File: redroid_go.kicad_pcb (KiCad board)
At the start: 2 copper layers, 70 x 95 mm, 100 parts, among them J1 USB4105-GF-A, J2 5051101892, J3 Conn_01x02_Pin, J4 Conn_01x10_Pin, Q1 UMH3N, Q2 PMOS, Q3 UMH3N, SW1 UP, SW10 A, SW11 SW_SPDT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

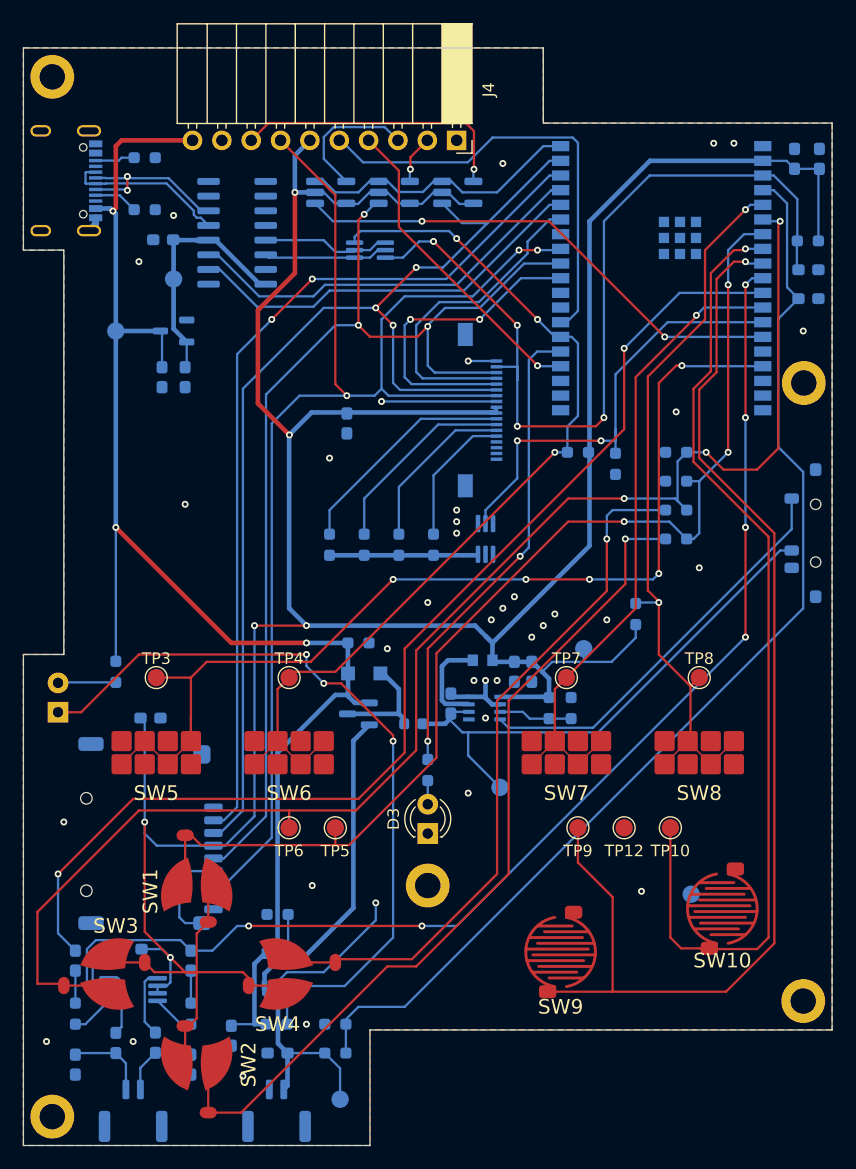
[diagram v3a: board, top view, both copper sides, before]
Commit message: Integrate feedback from JLCDFM
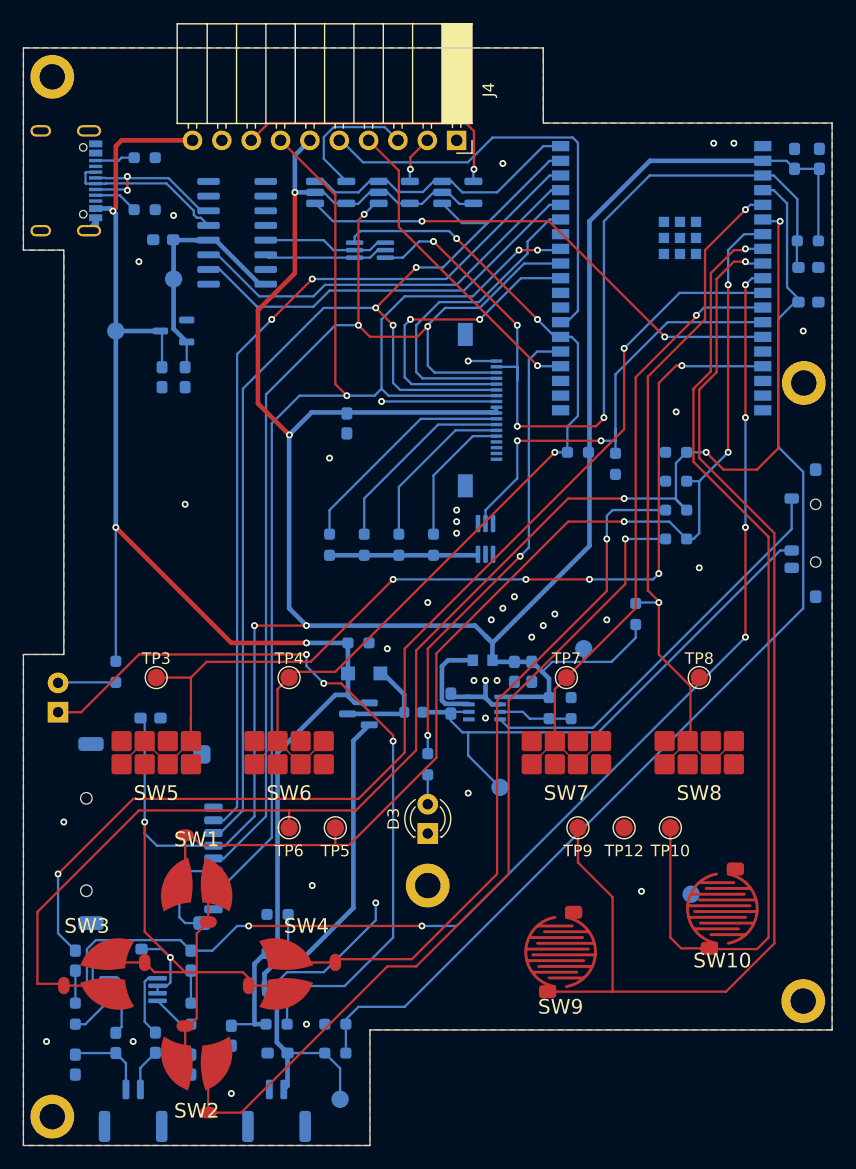
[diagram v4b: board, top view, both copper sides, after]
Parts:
- moved F1 1.00 mm to (162.2, 101.0)
- moved R18 0.50 mm to (163.5, 105.5)
- moved C20 0.30 mm to (196.4, 65.5)
- moved C9 0.20 mm to (196.4, 62.5)
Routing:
- net Net-(D1-K): track 9.79 -> 8.47 mm
- net IO34: track 120.9 -> 122.1 mm
- net Net-(SW11-B): track 47.6 -> 46.9 mm
- net IO2: track 41.3 -> 40.8 mm
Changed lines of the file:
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@@
 			(drillshape 0)
 			(scaleselection 1)
-			(outputdirectory "/tmp/redroid_go/")
+			(outputdirectory "/tmp/gerber/")
 		)
 	)
@@
 		(at 143.5 130.655 90)
 		(property "Reference" "SW2"
-			(at -0.845 4.5 90)
+			(at -4.845 0 180)
 			(layer "F.SilkS")
 			(effects
@@
 		(at 143.5 116.655 -90)
 		(property "Reference" "SW1"
-			(at -0.155 4 90)
+			(at -4.655 0 180)
 			(layer "F.SilkS")
 			(effects
@@
 		(at 136.5 123.655)
 		(property "Reference" "SW3"
-			(at 0 -4.155 0)
+			(at -2.5 -4.155 0)
 			(layer "F.SilkS")
 			(effects
@@
 		(at 150.5 123.655 180)
 		(property "Reference" "SW4"
-			(at 0 -4.345 0)
+			(at -2.5 4.155 0)
 			(layer "F.SilkS")
 			(effects
@@
 	(footprint "Capacitor_SMD:C_0603_1608Metric_Pad1.08x0.95mm_HandSolder"
 		(layer "B.Cu")
-		(at 196.45 65.2)
+		(at 196.45 65.5)
 		(descr "Capacitor SMD 0603 (1608 Metric), square (rectangular) end terminal, IPC_7351 nominal with elongated pad for handsoldering. (Body size source: IPC-SM-782 page 76, https://www.pcb-3d.com/wordpress/wp-content/uploads/ipc-sm-782a_amendment_1_and_2.pdf), generated with kicad-footprint-generator")
 		(tags "capacitor handsolder")
@@
 		(tags "CFP3 SOD-123W")
 		(property "Reference" "D1"
-			(at 3 -0.109551 0)
+			(at -3.5 0.640449 0)
 			(layer "B.SilkS")
 			(effects
@@
 		(tags "connector JST GH horizontal")
 		(property "Reference" "BT1"
-			(at 0 -1 0)
+			(at 4.9125 -1.5 0)
 			(layer "B.SilkS")
 			(effects
@@
 	(footprint "Capacitor_SMD:C_0603_1608Metric_Pad1.08x0.95mm_HandSolder"
 		(layer "B.Cu")
-		(at 196.45 62.7)
+		(at 196.45 62.5)
 		(descr "Capacitor SMD 0603 (1608 Metric), square (rectangular) end terminal, IPC_7351 nominal with elongated pad for handsoldering. (Body size source: IPC-SM-782 page 76, https://www.pcb-3d.com/wordpress/wp-content/uploads/ipc-sm-782a_amendment_1_and_2.pdf), generated with kicad-footprint-generator")
 		(tags "capacitor handsolder")
@@
 	(footprint "Fuse:Fuse_0603_1608Metric"
 		(layer "B.Cu")
-		(at 162.25 102)
+		(at 162.25 101)
 		(descr "Fuse SMD 0603 (1608 Metric), square (rectangular) end terminal, IPC_7351 nominal, (Body size source: http://www.tortai-tech.com/upload/download/2011102023233369053.pdf), generated with kicad-footprint-generator")
 		(tags "fuse")
@@
 		(tags "capacitor handsolder")
 		(property "Reference" "C4"
-			(at -2 0 0)
+			(at -2.8 0 90)
 			(layer "B.SilkS")
 			(effects
@@
 	(footprint "Resistor_SMD:R_0603_1608Metric_Pad0.98x0.95mm_HandSolder"
 		(layer "B.Cu")
-		(at 163.5 106 90)
+		(at 163.5 105.5 90)
 		(descr "Resistor SMD 0603 (1608 Metric), square (rectangular) end terminal, IPC_7351 nominal with elongated pad for handsoldering. (Body size source: IPC-SM-782 page 72, https://www.pcb-3d.com/wordpress/wp-content/uploads/ipc-sm-782a_amendment_1_and_2.pdf), generated with kicad-footprint-generator")
 		(tags "resistor handsolder")
@@
 		(tags "connector JST GH horizontal")
 		(property "Reference" "J3"
-			(at 0 -0.5 0)
+			(at -4.5 1 0)
 			(layer "B.SilkS")
 			(effects
@@
 	)
 	(via
-		(at 147.5 132.5)
+		(at 146.5 134)
 		(size 0.6)
 		(drill 0.3)
@@
 	)
 	(segment
-		(start 150.5375 129.675)
-		(end 150.5375 126.5375)
+		(start 150.4375 126.4375)
+		(end 149.373209 125.373209)
+		(width 0.4)
+		(layer "B.Cu")
+		(net 2)
+	)
+	(segment
+		(start 150.4375 129.575)
+		(end 150.4375 126.4375)
 		(width 0.4)
 		(layer "B.Cu")
@@
 	)
 	(segment
-		(start 151.3625 130.5)
-		(end 150.5375 129.675)
-		(width 0.4)
-		(layer "B.Cu")
-		(net 2)
-	)
-	(segment
 		(start 157.0625 117.9375)
 		(end 152 123)
@@
 	)
 	(segment
-		(start 150.5375 126.5375)
-		(end 149.373209 125.373209)
+		(start 152 123)
+		(end 150 123)
 		(width 0.4)
 		(layer "B.Cu")
@@
 	)
 	(segment
-		(start 152 123)
-		(end 150 123)
+		(start 150.4375 129.575)
+		(end 151.3625 130.5)
 		(width 0.4)
 		(layer "B.Cu")
@@
 	)
 	(segment
-		(start 165.5 101.5)
-		(end 165.5 101.1125)
-		(width 0.4)
-		(layer "B.Cu")
-		(net 4)
-	)
-	(segment
-		(start 165 102)
-		(end 165.5 101.5)
-		(width 0.4)
-		(layer "B.Cu")
-		(net 4)
-	)
-	(segment
 		(start 167 104.75)
 		(end 167 102.740449)
@@
 	)
 	(segment
-		(start 163.0375 102)
-		(end 165 102)
-		(width 0.4)
+		(start 165.64705 100.96545)
+		(end 165.5 101.1125)
+		(width 0.2)
 		(layer "B.Cu")
 		(net 4)
 	)
 	(segment
-		(start 165.64705 100.96545)
-		(end 165.5 101.1125)
-		(width 0.2)
+		(start 163.0375 101)
+		(end 165 101)
+		(width 0.4)
 		(layer "B.Cu")
 		(net 4)
@@
 	)
 	(segment
+		(start 165.5 101.5)
+		(end 165.5 101.1125)
+		(width 0.4)
+		(layer "B.Cu")
+		(net 4)
+	)
+	(segment
 		(start 136.5 52)
 		(end 137 51.5)
@@
 	(segment
 		(start 161 101.140449)
-		(end 161.4625 101.602949)
+		(end 156.5625 101.140449)
 		(width 0.4)
 		(layer "B.Cu")
@@
 	)
 	(segment
-		(start 161.4625 101.602949)
-		(end 161.4625 102)
-		(width 0.2)
-		(layer "B.Cu")
-		(net 14)
-	)
-	(segment
-		(start 161 101.140449)
-		(end 156.5625 101.140449)
+		(start 159.640449 97.640449)
+		(end 161.4625 99.4625)
 		(width 0.4)
 		(layer "B.Cu")
@@
 	)
 	(segment
-		(start 159.640449 97.640449)
-		(end 161 99)
-		(width 0.4)
-		(layer "B.Cu")
-		(net 14)
-	)
-	(segment
-		(start 161 99)
-		(end 161 101.140449)
+		(start 161.4625 99.4625)
+		(end 161.4625 100.677949)
 		(width 0.4)
 		(layer "B.Cu")
@@
 	)
 	(segment
-		(start 155.5 61.15)
-		(end 154.485 60.135)
+		(start 155.35 61)
+		(end 157.02 61)
 		(width 0.2)
 		(layer "B.Cu")
@@
 	)
 	(segment
-		(start 155.5 61.15)
-		(end 157.17 61.15)
+		(start 154.485 60.135)
+		(end 155.35 61)
 		(width 0.2)
 		(layer "B.Cu")
@@
 	)
 	(segment
-		(start 154.485 60.135)
-		(end 149.475 60.135)
+		(start 149.475 60.135)
+		(end 154.485 60.135)
 		(width 0.2)
 		(layer "B.Cu")
@@
 	(segment
 		(start 184.9125 82.5)
-		(end 185.125 82.7125)
+		(end 185.9125 83.5)
 		(width 0.2)
 		(layer "B.Cu")
@@
 	)
 	(segment
-		(start 185.125 79.2875)
+		(start 184.98125 79.43125)
 		(end 185.9125 78.5)
 		(width 0.2)
@@
 	)
 	(segment
-		(start 185.125 82.7125)
-		(end 185.125 79.2875)
+		(start 185.9125 83.5)
+		(end 184.98125 82.56875)
+		(width 0.2)
+		(layer "B.Cu")
+		(net 58)
+	)
+	(segment
+		(start 184.98125 82.56875)
+		(end 184.98125 79.43125)
 		(width 0.2)
 		(layer "B.Cu")
@@
 	)
 	(segment
-		(start 185.9125 83.5)
-		(end 185.125 82.7125)
-		(width 0.2)
-		(layer "B.Cu")
-		(net 58)
-	)
-	(segment
 		(start 180.5 82.5)
 		(end 184.9125 82.5)
@@
 	)
 	(segment
-		(start 163.5 103.5)
-		(end 163.5 95.5)
+		(start 163.5 95.5)
+		(end 171.5 87.5)
 		(width 0.2)
 		(layer "F.Cu")
@@
 	)
 	(segment
-		(start 163.5 95.5)
-		(end 171.5 87.5)
+		(start 163.5 103)
+		(end 163.5 95.5)
 		(width 0.2)
 		(layer "F.Cu")
@@
 	)
 	(via
-		(at 163.5 103.5)
+		(at 163.5 103)
 		(size 0.6)
 		(drill 0.3)
@@
 	)
 	(segment
-		(start 163.5 103.5)
-		(end 163.5 105.0875)
+		(start 163.5 103)
+		(end 163.5 104.5875)
 		(width 0.2)
 		(layer "B.Cu")

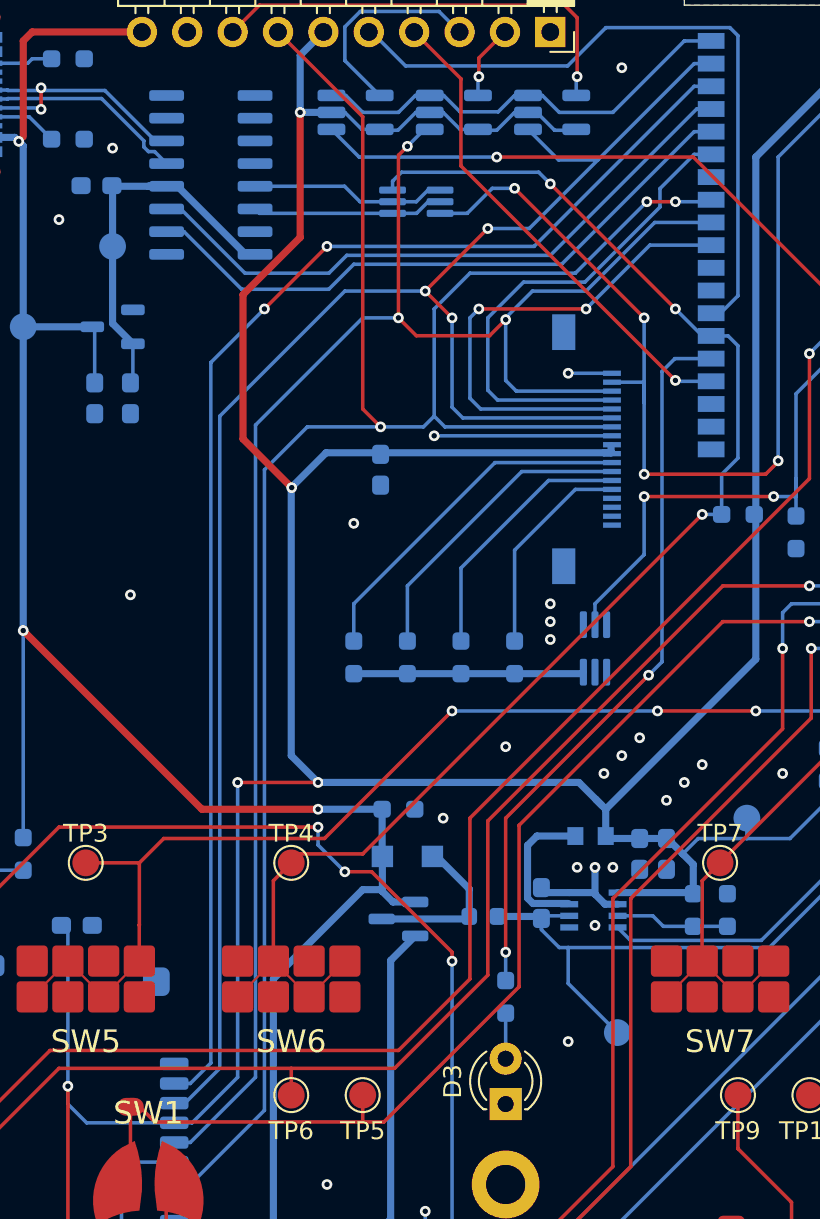
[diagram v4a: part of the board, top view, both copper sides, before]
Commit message: Update 3v3 trace
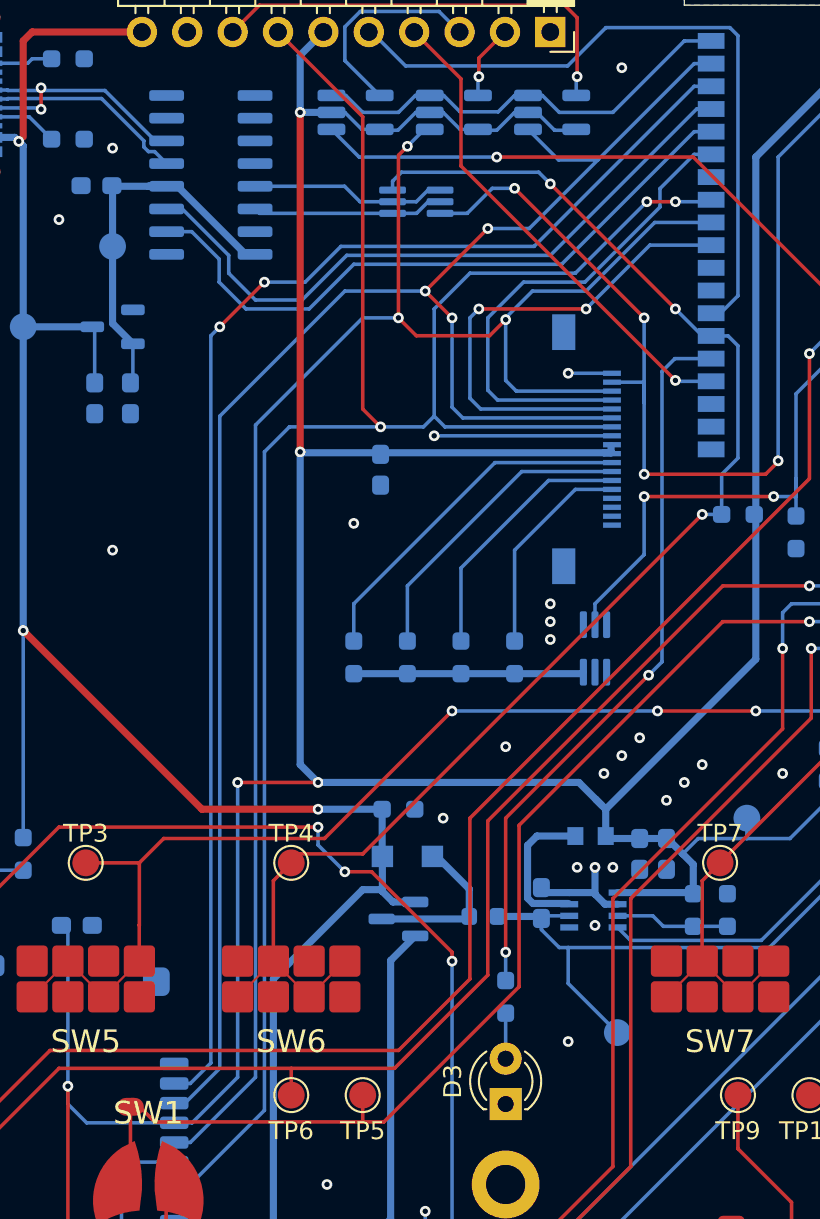
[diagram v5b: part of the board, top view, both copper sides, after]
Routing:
- net P3V3: track 275.5 -> 271.6 mm
- net TX0: track 35.8 -> 37.6 mm
- net RX0: track 35.5 -> 37.1 mm
- net CS1: track 76.1 -> 77.0 mm
- net MISO: track 112.0 -> 112.6 mm

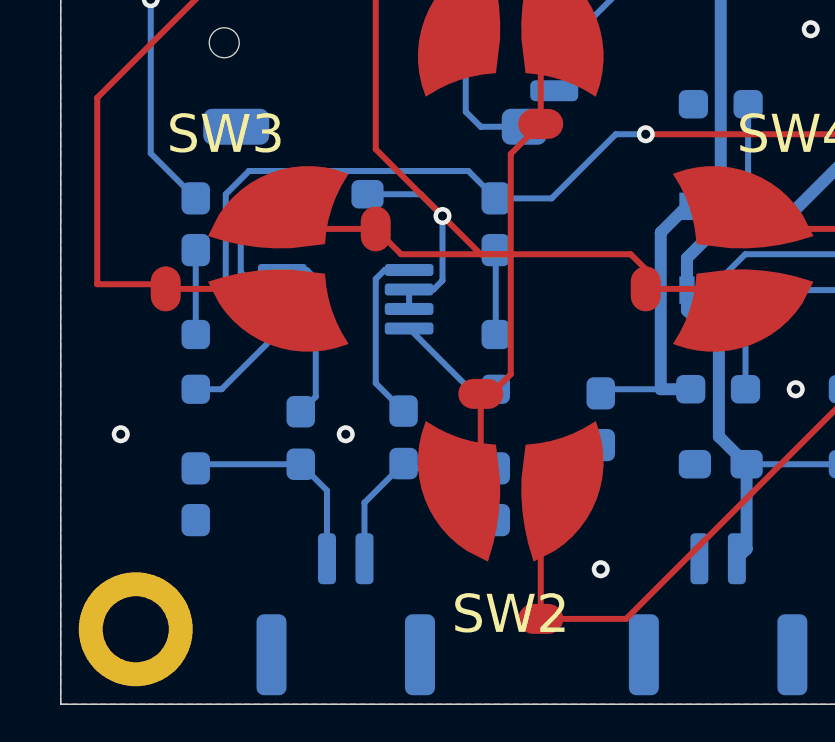
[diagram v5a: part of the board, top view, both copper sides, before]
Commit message: Improve symmetry of audio components
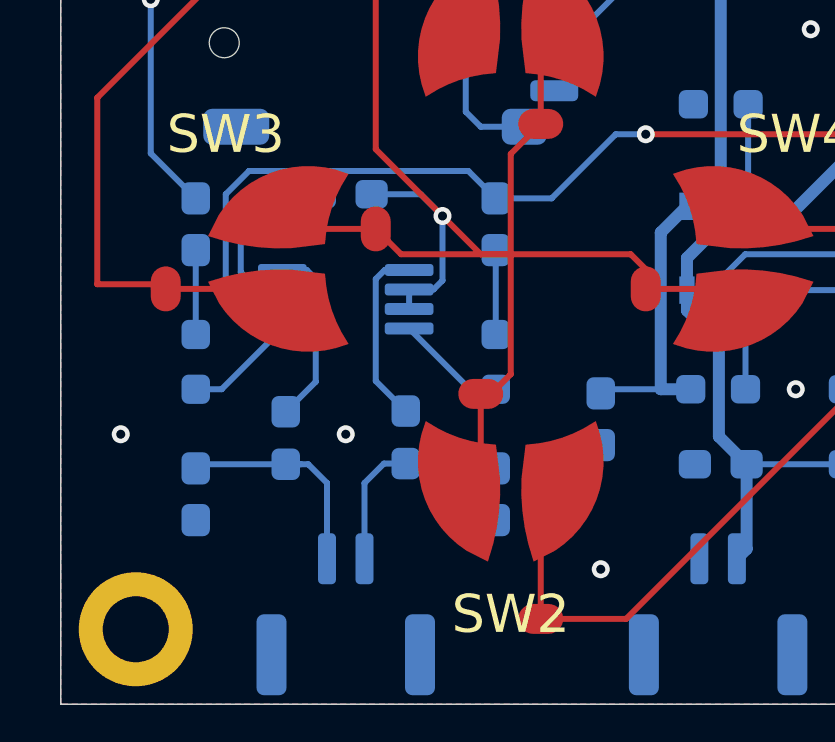
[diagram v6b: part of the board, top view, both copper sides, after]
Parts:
- moved FB2 0.50 mm to (136.0, 129.6)
- moved C13 0.14 mm to (138.0, 121.5)
- moved FB1 0.07 mm to (140.0, 129.6)
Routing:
- net Net-(J3-Pin_2): track 7.30 -> 7.95 mm
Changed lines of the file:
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@@
 	(footprint "Inductor_SMD:L_0603_1608Metric_Pad1.05x0.95mm_HandSolder"
 		(layer "B.Cu")
-		(at 136.5 129.625 90)
+		(at 136 129.625 90)
 		(descr "Inductor SMD 0603 (1608 Metric), square (rectangular) end terminal, IPC_7351 nominal with elongated pad for handsoldering. (Body size source: http://www.tortai-tech.com/upload/download/2011102023233369053.pdf), generated with kicad-footprint-generator")
 		(tags "inductor handsolder")
@@
 	(footprint "Inductor_SMD:L_0603_1608Metric_Pad1.05x0.95mm_HandSolder"
 		(layer "B.Cu")
-		(at 139.927589 129.601973 90)
+		(at 140 129.601973 90)
 		(descr "Inductor SMD 0603 (1608 Metric), square (rectangular) end terminal, IPC_7351 nominal with elongated pad for handsoldering. (Body size source: http://www.tortai-tech.com/upload/download/2011102023233369053.pdf), generated with kicad-footprint-generator")
 		(tags "inductor handsolder")
@@
 	(footprint "Capacitor_SMD:C_0603_1608Metric_Pad1.08x0.95mm_HandSolder"
 		(layer "B.Cu")
-		(at 137.8625 121.5 180)
+		(at 138 121.5 180)
 		(descr "Capacitor SMD 0603 (1608 Metric), square (rectangular) end terminal, IPC_7351 nominal with elongated pad for handsoldering. (Body size source: IPC-SM-782 page 76, https://www.pcb-3d.com/wordpress/wp-content/uploads/ipc-sm-782a_amendment_1_and_2.pdf), generated with kicad-footprint-generator")
 		(tags "capacitor handsolder")
@@
 	(segment
 		(start 143 130.6375)
-		(end 140.088116 130.6375)
+		(end 142.839473 130.476973)
 		(width 0.2)
 		(layer "B.Cu")
@@
 	)
 	(segment
-		(start 138.625 131.779562)
+		(start 142.839473 130.476973)
 		(end 139.927589 130.476973)
 		(width 0.2)
@@
 	)
 	(segment
-		(start 140.088116 130.6375)
-		(end 139.927589 130.476973)
+		(start 138.625 131.125)
+		(end 138.625 133.65)
+		(width 0.2)
+		(layer "B.Cu")
+		(net 11)
+	)
+	(segment
+		(start 140 130.476973)
+		(end 139.273027 130.476973)
 		(width 0.2)
 		(layer "B.Cu")
@@
 	)
 	(segment
-		(start 138.625 133.65)
-		(end 138.625 131.779562)
+		(start 139.273027 130.476973)
+		(end 138.625 131.125)
 		(width 0.2)
 		(layer "B.Cu")
@@
 	)
 	(segment
-		(start 137.375 133.65)
-		(end 137.375 131.375)
+		(start 136.75 130.5)
+		(end 137.375 131.125)
 		(width 0.2)
 		(layer "B.Cu")
@@
 	)
 	(segment
-		(start 137.375 131.375)
-		(end 136.5 130.5)
+		(start 136 130.5)
+		(end 136.75 130.5)
+		(width 0.2)
+		(layer "B.Cu")
+		(net 12)
+	)
+	(segment
+		(start 137.375 131.125)
+		(end 137.375 133.65)
 		(width 0.2)
 		(layer "B.Cu")
@@
 	)
 	(segment
-		(start 139.927589 128.726973)
-		(end 139 127.799384)
+		(start 139.300001 124.025)
+		(end 140.1125 124.025)
 		(width 0.2)
 		(layer "B.Cu")
@@
 	)
 	(segment
-		(start 139.300001 124.025)
-		(end 140.1125 124.025)
+		(start 139 124.325001)
+		(end 139.300001 124.025)
 		(width 0.2)
 		(layer "B.Cu")
@@
 	)
 	(segment
-		(start 139 127.799384)
-		(end 139 124.325001)
+		(start 139 127.726973)
+		(end 140 128.726973)
 		(width 0.2)
 		(layer "B.Cu")
@@
 	(segment
 		(start 139 124.325001)
-		(end 139.300001 124.025)
+		(end 139 127.726973)
 		(width 0.2)
 		(layer "B.Cu")
@@
 	)
 	(segment
-		(start 136.699999 124.025)
-		(end 135.8875 124.025)
+		(start 137 127.75)
+		(end 136 128.75)
 		(width 0.2)
 		(layer "B.Cu")
@@
 	)
 	(segment
-		(start 137 128.25)
-		(end 137 124.325001)
+		(start 136.699999 124.025)
+		(end 135.8875 124.025)
 		(width 0.2)
 		(layer "B.Cu")
@@
 	)
 	(segment
-		(start 136.5 128.75)
-		(end 137 128.25)
+		(start 137 124.325001)
+		(end 137 127.75)
 		(width 0.2)
 		(layer "B.Cu")
